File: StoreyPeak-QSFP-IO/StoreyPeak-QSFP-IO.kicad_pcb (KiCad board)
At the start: 2 copper layers, 30.1 x 69.8 mm, 28 parts, among them U1 QSFP_PCB-QSFP, U3 CH340G, X1 X322512MSB4SI

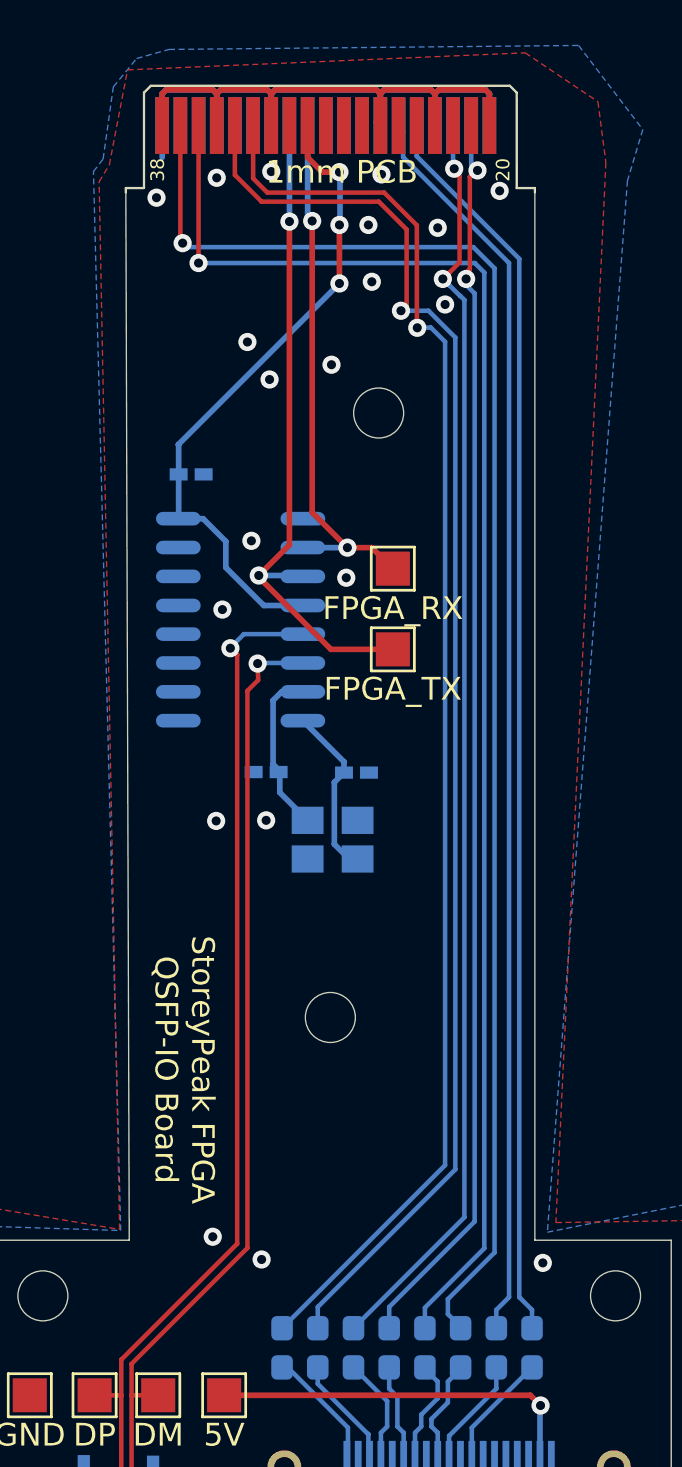
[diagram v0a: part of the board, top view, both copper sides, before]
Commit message: Change QSFP->HDMI mapping for better routing, skew match diffpairs
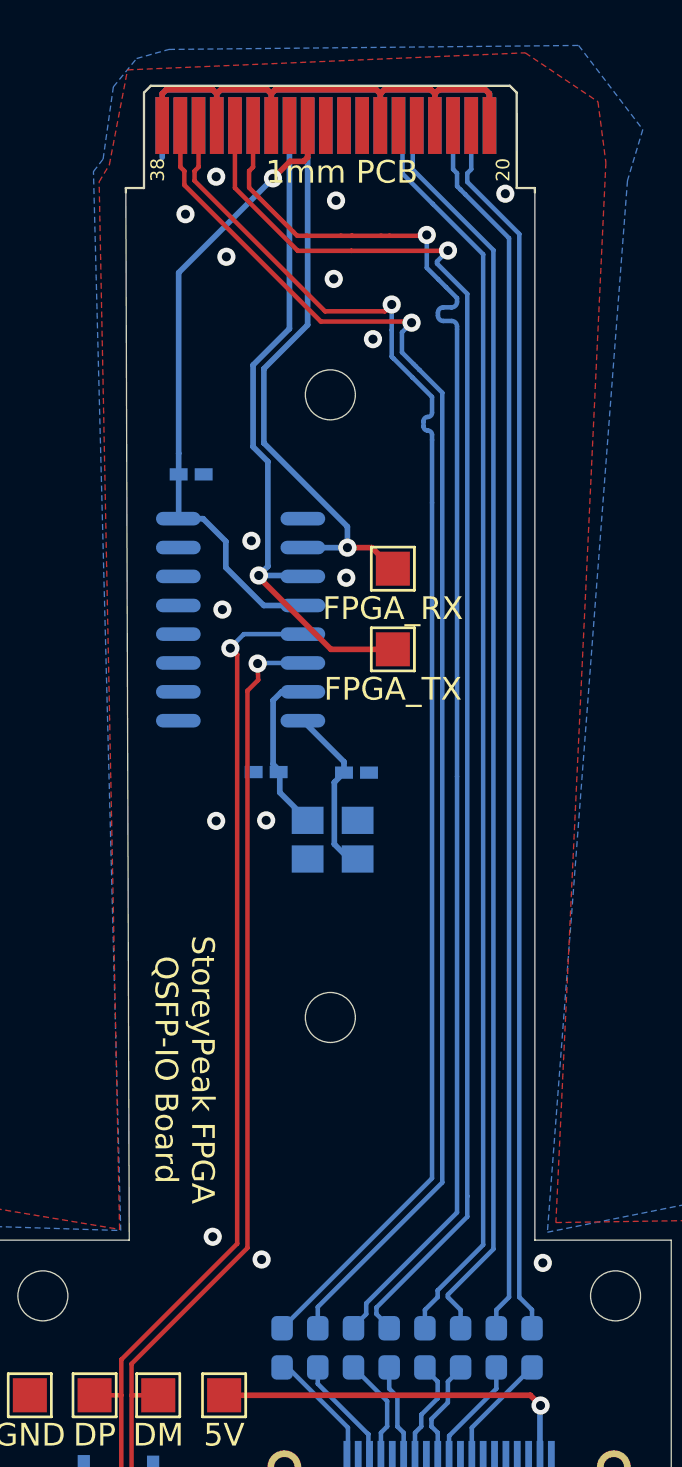
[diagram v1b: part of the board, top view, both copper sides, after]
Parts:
- moved H2 27.4 mm to (162.0, 76.8)
- moved H1 26.7 mm to (162.0, 104.2)
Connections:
- net Net-(U1-SCL) renamed FPGA_RX
- net Net-(U1-SDA) renamed FPGA_TX
- C10 pad 1: /QSFP_CLK- -> QSFP_CLK+
- C3 pad 1: /QSFP_D0- -> QSFP_D0-
- C4 pad 1: /QSFP_D0+ -> QSFP_D0+
- C5 pad 1: /QSFP_D1- -> QSFP_D1-
- C6 pad 1: /QSFP_D1+ -> QSFP_D1+
- C7 pad 1: /QSFP_D2- -> QSFP_D2-
- C8 pad 1: /QSFP_D2+ -> QSFP_D2+
- C9 pad 1: /QSFP_CLK+ -> QSFP_CLK-
- U1 pad 2: /QSFP_D1- -> QSFP_CLK-
- U1 pad 3: /QSFP_D1+ -> QSFP_CLK+
- U1 pad 33: /QSFP_D2+ -> QSFP_D1+
- U1 pad 34: /QSFP_D2- -> QSFP_D1-
- U1 pad 36: /QSFP_D0+ -> QSFP_D2+
- U1 pad 37: /QSFP_D0- -> QSFP_D2-
- U1 pad 5: /QSFP_CLK+ -> QSFP_D0-
- U1 pad 6: /QSFP_CLK- -> QSFP_D0+
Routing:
- net /QSFP_D0-: track 67.2 -> 0.00 mm, vias 1 -> 0
- net /QSFP_D0+: track 66.4 -> 0.00 mm, vias 1 -> 0
- net /QSFP_D2-: track 63.5 -> 0.00 mm, vias 1 -> 0
- net QSFP_D1-: track 0.00 -> 63.4 mm, vias 0 -> 1
- net QSFP_D1+: track 0.00 -> 63.3 mm, vias 0 -> 1
- net /QSFP_D2+: track 62.8 -> 0.00 mm, vias 1 -> 0
- net QSFP_D2-: track 0.00 -> 62.7 mm, vias 0 -> 1
- net QSFP_D2+: track 0.00 -> 62.6 mm, vias 0 -> 1
- net /QSFP_D1+: track 55.8 -> 0.00 mm, vias 2 -> 0
- net QSFP_D0-: track 0.00 -> 55.5 mm
- net QSFP_D0+: track 0.00 -> 55.5 mm
- net /QSFP_D1-: track 55.1 -> 0.00 mm, vias 2 -> 0
- net /QSFP_CLK-: track 55.1 -> 0.00 mm
- net /QSFP_CLK+: track 55.0 -> 0.00 mm
- net QSFP_CLK+: track 0.00 -> 54.1 mm
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
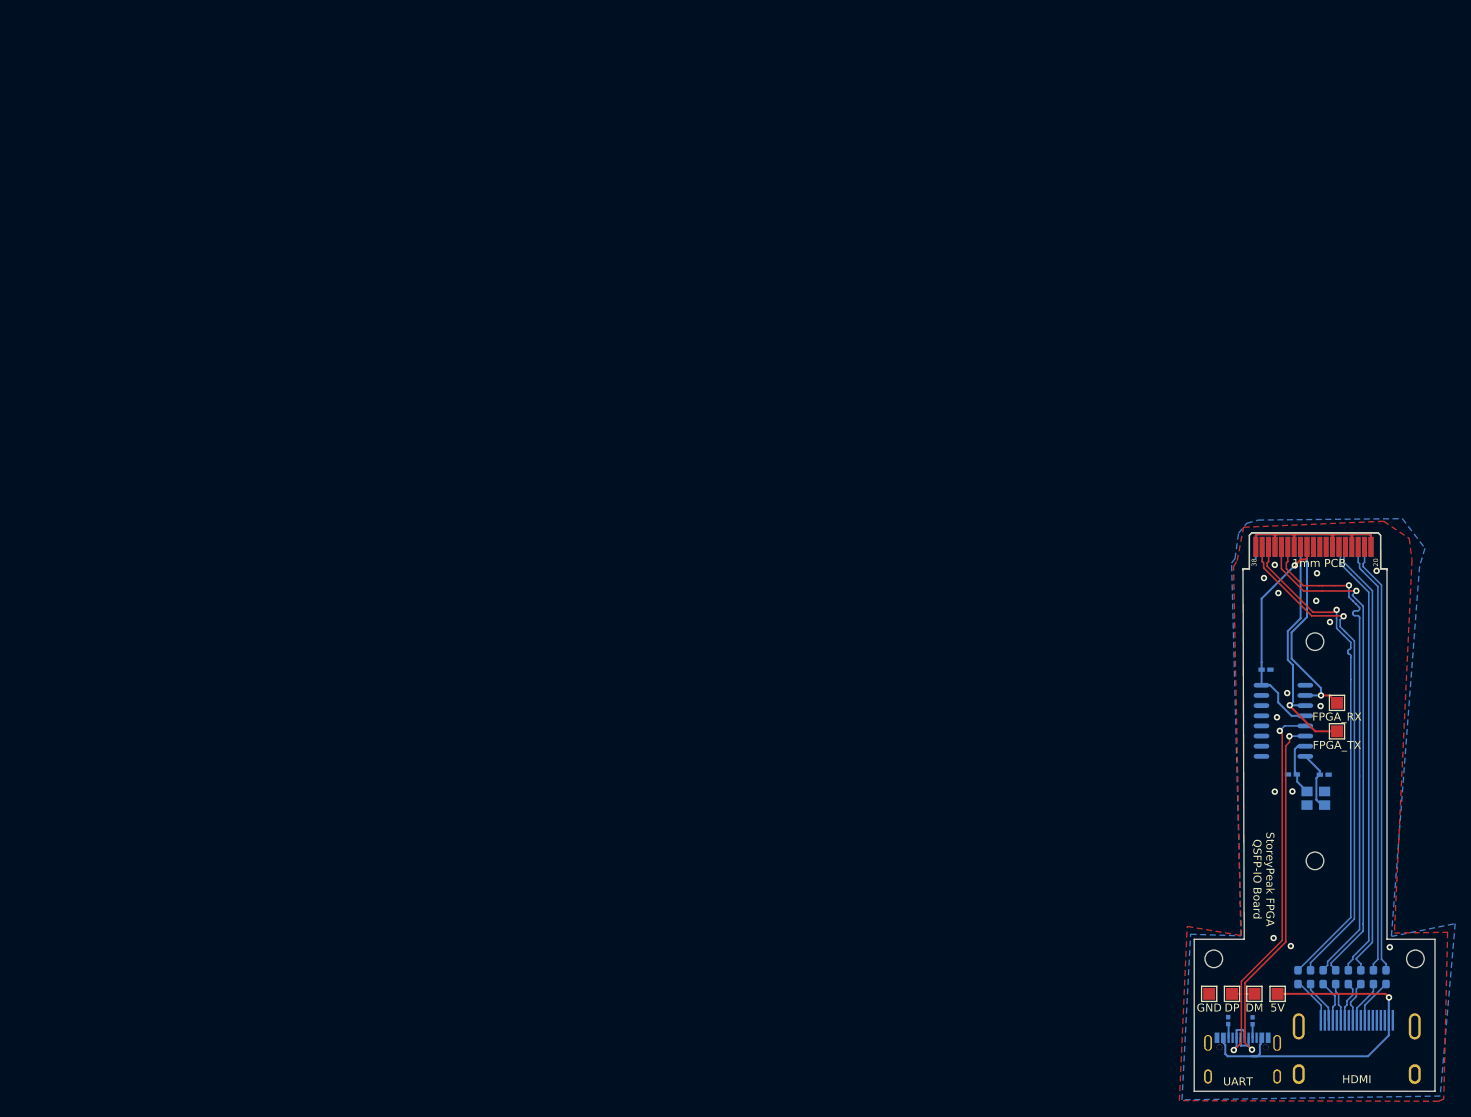
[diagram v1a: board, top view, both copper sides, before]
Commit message: Add GND pad next to UART pads, reroute 5V pad to avoid breaking GND plane below HDMI signals
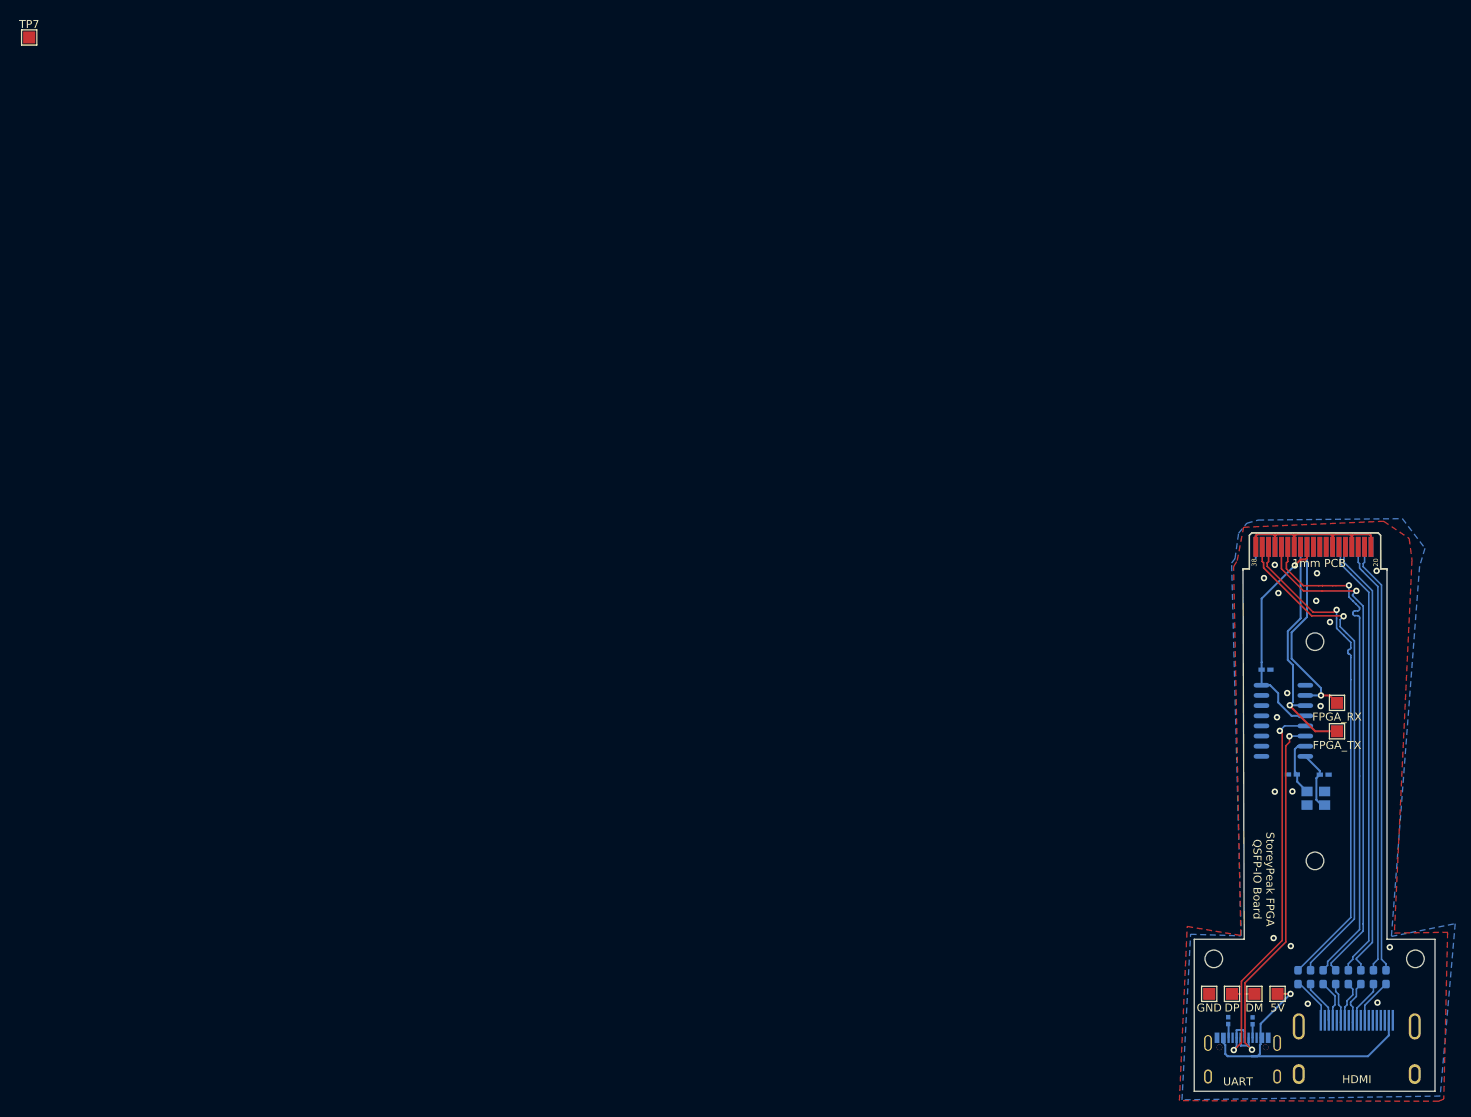
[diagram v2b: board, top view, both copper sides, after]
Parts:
- added TP7: GND, TestPoint:TestPoint_Pad_1.5x1.5mm, F.Cu at (1.27, 1.27)
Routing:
- net +5V: track 45.7 -> 37.2 mm
- net GND: vias 15 -> 17
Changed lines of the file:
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@@
 	(footprint "TestPoint:TestPoint_Pad_1.5x1.5mm"
 		(layer "F.Cu")
+		(at 1.275 1.275)
+		(descr "SMD rectangular pad as test Point, square 1.5mm side length")
+		(tags "test point SMD pad rectangle square")
+		(property "Reference" "TP7"
+			(at 0 -1.648 0)
+			(layer "F.SilkS")
+			(effects
+				(font
+					(size 1 1)
+					(thickness 0.15)
+				)
+			)
+		)
+		(property "Value" "GND"
+			(at 0 1.75 0)
+			(layer "F.Fab")
+			(effects
+				(font
+					(size 1 1)
+					(thickness 0.15)
+				)
+			)
+		)
+		(property "Footprint" "TestPoint:TestPoint_Pad_1.5x1.5mm"
+			(at 0 0 0)
+			(unlocked yes)
+			(layer "F.Fab")
+			(hide yes)
+			(effects
+				(font
+					(size 1.27 1.27)
+					(thickness 0.15)
+				)
+			)
+		)
+		(property "Datasheet" ""
+			(at 0 0 0)
+			(unlocked yes)
+			(layer "F.Fab")
+			(hide yes)
+			(effects
+				(font
+					(size 1.27 1.27)
+					(thickness 0.15)
+				)
+			)
+		)
+		(property "Description" "test point"
+			(at 0 0 0)
+			(unlocked yes)
+			(layer "F.Fab")
+			(hide yes)
+			(effects
+				(font
+					(size 1.27 1.27)
+					(thickness 0.15)
+				)
+			)
+		)
+		(property ki_fp_filters "Pin* Test*")
+		(sheetname "Root")
+		(sheetfile "StoreyPeak-QSFP-IO.kicad_sch")
+		(attr exclude_from_pos_files)
+		(fp_line
+			(start -0.95 -0.95)
+			(end 0.95 -0.95)
+			(stroke
+				(width 0.12)
+				(type solid)
+			)
+			(layer "F.SilkS")
+		)
+		(fp_line
+			(start -0.95 0.95)
+			(end -0.95 -0.95)
+			(stroke
+				(width 0.12)
+				(type solid)
+			)
+			(layer "F.SilkS")
+		)
+		(fp_line
+			(start 0.95 -0.95)
+			(end 0.95 0.95)
+			(stroke
+				(width 0.12)
+				(type solid)
+			)
+			(layer "F.SilkS")
+		)
+		(fp_line
+			(start 0.95 0.95)
+			(end -0.95 0.95)
+			(stroke
+				(width 0.12)
+				(type solid)
+			)
+			(layer "F.SilkS")
+		)
+		(fp_line
+			(start -1.25 -1.25)
+			(end -1.25 1.25)
+			(stroke
+				(width 0.05)
+				(type solid)
+			)
+			(layer "F.CrtYd")
+		)
+		(fp_line
+			(start -1.25 -1.25)
+			(end 1.25 -1.25)
+			(stroke
+				(width 0.05)
+				(type solid)
+			)
+			(layer "F.CrtYd")
+		)
+		(fp_line
+			(start 1.25 1.25)
+			(end -1.25 1.25)
+			(stroke
+				(width 0.05)
+				(type solid)
+			)
+			(layer "F.CrtYd")
+		)
+		(fp_line
+			(start 1.25 1.25)
+			(end 1.25 -1.25)
+			(stroke
+				(width 0.05)
+				(type solid)
+			)
+			(layer "F.CrtYd")
+		)
+		(fp_text user "${REFERENCE}"
+			(at 0 -1.65 0)
+			(layer "F.Fab")
+			(effects
+				(font
+					(size 1 1)
+					(thickness 0.15)
+				)
+			)
+		)
+		(pad "1" smd rect
+			(at 0 0)
+			(size 1.5 1.5)
+			(layers "F.Cu" "F.Mask")
+			(net 1 "GND")
+			(pinfunction "1")
+			(pintype "passive")
+		)
+	)
+	(footprint "TestPoint:TestPoint_Pad_1.5x1.5mm"
+		(layer "F.Cu")
 		(at 164.75 88)
 		(descr "SMD rectangular pad as test Point, square 1.5mm side length")
@@
 	)
 	(via
+		(at 169.81 121.92)
+		(size 0.8)
+		(drill 0.4)
+		(layers "F.Cu" "B.Cu")
+		(free yes)
+		(net 1)
+	)
+	(via
 		(at 163.875 74.35)
 		(size 0.8)
@@
 	)
 	(via
+		(at 161.1 122.06)
+		(size 0.8)
+		(drill 0.4)
+		(layers "F.Cu" "B.Cu")
+		(free yes)
+		(net 1)
+	)
+	(via
 		(at 158.525 83.225)
 		(size 0.8)
@@
 	)
 	(segment
-		(start 171.25 121.25)
-		(end 171.25 121.275)
-		(width 0.25)
-		(layer "F.Cu")
-		(net 2)
-	)
-	(segment
-		(start 171.25 121.275)
-		(end 171.25 121.3)
-		(width 0.25)
-		(layer "F.Cu")
-		(net 2)
-	)
-	(segment
-		(start 170.8 120.825)
+		(start 157.33 120.83)
 		(end 157.325 120.825)
 		(width 0.25)
@@
 	)
 	(segment
-		(start 171.25 121.3)
-		(end 171.3 121.3)
-		(width 0.25)
-		(layer "F.Cu")
-		(net 2)
-	)
-	(segment
-		(start 171.3 121.3)
-		(end 171.25 121.25)
-		(width 0.25)
-		(layer "F.Cu")
-		(net 2)
-	)
-	(segment
-		(start 171.25 121.275)
-		(end 170.8 120.825)
+		(start 158.94 120.83)
+		(end 157.33 120.83)
 		(width 0.25)
 		(layer "F.Cu")
@@
 	)
 	(via
-		(at 171.25 121.275)
+		(at 158.94 120.83)
 		(size 0.8)
 		(drill 0.4)
@@
 	)
 	(segment
-		(start 171.25 121.3)
-		(end 171.225 121.325)
-		(width 0.25)
-		(layer "B.Cu")
-		(net 2)
-	)
-	(segment
 		(start 155.115 127.202195)
 		(end 155.2 127.117195)
@@
 	)
 	(segment
-		(start 171.225 121.325)
-		(end 171.225 124.1325)
-		(width 0.25)
-		(layer "B.Cu")
-		(net 2)
-	)
-	(segment
 		(start 150.4 126.817195)
 		(end 150.785 127.202195)
@@
 	)
 	(segment
+		(start 158.94 120.83)
+		(end 155.2 124.57)
+		(width 0.25)
+		(layer "B.Cu")
+		(net 2)
+	)
+	(segment
 		(start 150.4 126.3225)
 		(end 150.4 126.817195)
 		(width 0.25)
 		(layer "B.Cu")
+		(net 2)
+	)
+	(segment
+		(start 155.2 124.57)
+		(end 155.2 126.3125)
+		(width 0.25)
+		(layer "B.Cu")
